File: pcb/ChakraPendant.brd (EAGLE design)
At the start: 25.4 x 25.4 mm, 12 parts

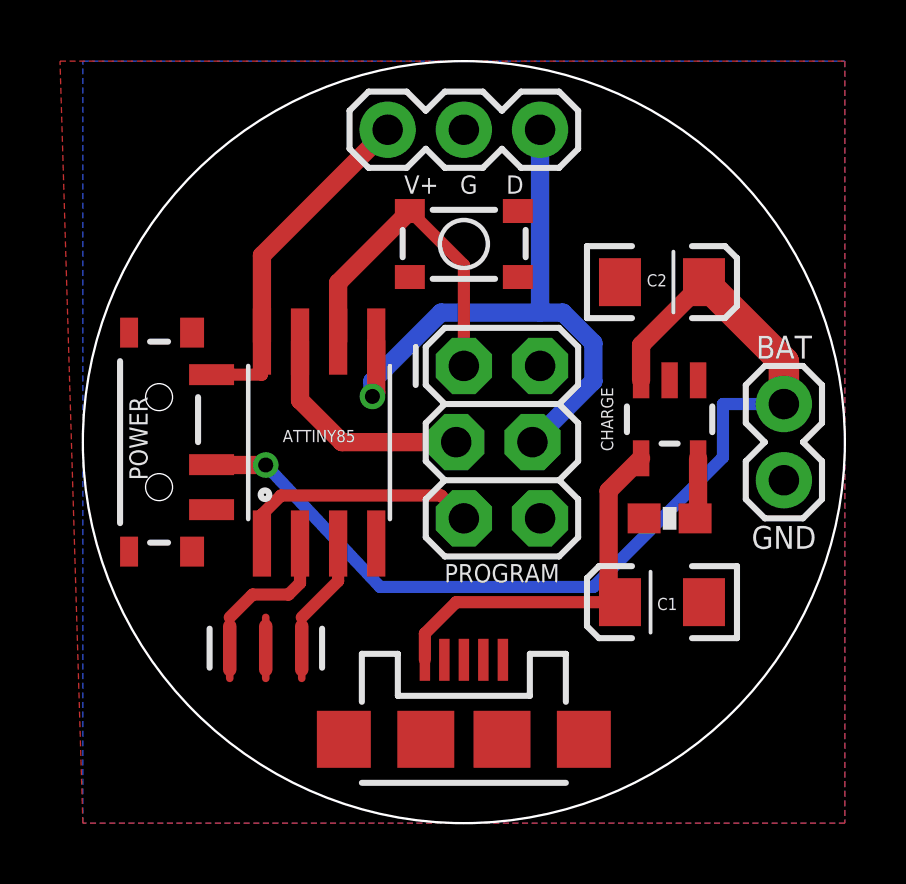
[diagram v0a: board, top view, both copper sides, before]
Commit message: Remove power switches. Add Charge LEDs. Change ISP header to pogopin programmer.
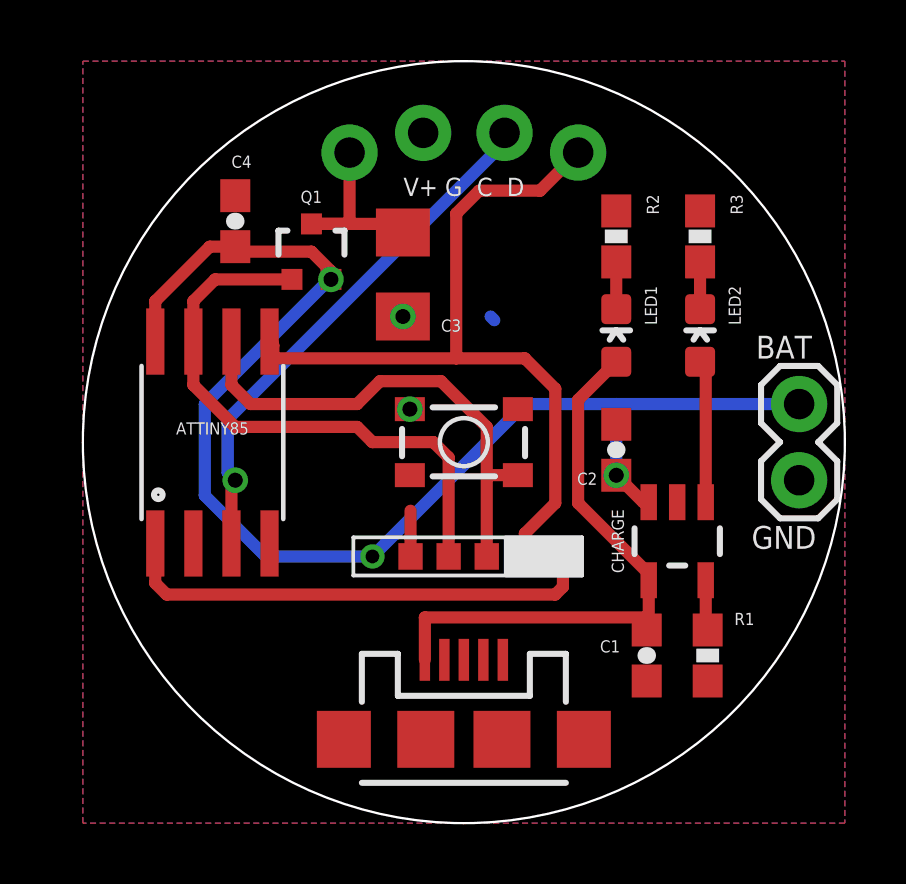
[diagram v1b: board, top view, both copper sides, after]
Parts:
- removed LEDS: (no value), SparkFun-Connectors:1X03
- removed MODE: SWITCH-MOMENTARY-2SMD-3, SparkFun-Electromechanical:TACTILE_SWITCH_SMD-3
- removed POWER: (no value), SparkFun-Electromechanical:SWITCH-SPST-SMD-A
- removed PROGRAM: (no value), SparkFun-Connectors:2X3_LOCK
- removed XTAL: 8MHZ, SparkFun-FreqCtrl:RESONATOR-SMD
- added C3: 22 uF, SparkFun-Passives:1206
- added C4: (no value), SparkFun-Passives:0603-CAP
- added LED1, LED2: (no value), SparkFun-LED:LED-0603
- added LEDPWR, LEDSIG: M021X02_NO_SILK, SparkFun-Connectors:1X02_NO_SILK
- added Q1: MOSFET-NCHANNEL2N7002PW, SparkFun-DiscreteSemi:SOT323
- added R2, R3: (no value), SparkFun-Passives:0603-RES
- added S2: SWITCH-MOMENTARY-2SMD-3, SparkFun-Electromechanical:TACTILE_SWITCH_SMD-3
- added U$1: POGOPIN-CONNWITHVIAS, Protofusion:POGOPROG-CONN-0H
- C1, C2: value 47 uF -> 4.7 uF; device SparkFun-Capacitors:EIA3216 -> SparkFun-Passives:0603-CAP
- moved C2 5.79 mm to (17.8, 12.4), turned to 90 degrees
- moved R1 4.75 mm to (20.8, 5.59), turned to 270 degrees
- moved CHARGE 4.07 mm to (19.8, 9.40)
- moved ATTINY85 3.56 mm to (4.32, 12.7)
- moved C1 1.85 mm to (18.8, 5.59), turned to 270 degrees
- moved BAT 0.51 mm to (23.9, 11.4)
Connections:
- removed net USBV+: C1.A, CHARGE.4, JP1.VBUS
- removed net VCC: ATTINY85.8, LEDS.1, POWER.3
- removed net XTAL1: ATTINY85.3, XTAL.1
- removed net XTAL2: ATTINY85.2, XTAL.3
- new net N$1: C3.1, LEDPWR.1, Q1.3
- new net N$2: C1.1, CHARGE.4, JP1.VBUS, LED1.A
- new net N$3: ATTINY85.3, LEDSIG.2
- new net N$4: LED1.C, R2.2
- new net N$5: LED2.C, R3.2
- new net N$7: CHARGE.1, LED2.A
- net BATTV+: now also ATTINY85.8, C2.1, C4.1, Q1.2, U$1.6; no longer C2.A, POWER.2
- net GND: now also C1.2, C2.2, C3.2, C4.2, LEDPWR.2, R2.1, R3.1, S2.4, U$1.5; no longer C1.C, C2.C, LEDS.2, MODE.4, PROGRAM.6, XTAL.2
- net PB0-MOSI: now also LEDSIG.1, U$1.2; no longer LEDS.3, PROGRAM.4
- net PB1-MISO: now also S2.1, U$1.3; no longer MODE.1, PROGRAM.1
- net PB2-SCK: now also Q1.1, U$1.4; no longer PROGRAM.3
- net PB5-RESET: now also U$1.1; no longer PROGRAM.5
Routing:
- net N$2: track 0.00 -> 19.7 mm
- net N$3: track 0.00 -> 17.7 mm, vias 0 -> 1
- net USBV+: track 13.2 -> 0.00 mm
- net VCC: track 11.6 -> 0.00 mm
- net PB2-SCK: track 7.74 -> 19.2 mm
- net BATTV+: track 33.7 -> 44.2 mm, vias 1 -> 2
- net PB5-RESET: track 8.27 -> 16.2 mm
- net N$1: track 0.00 -> 6.98 mm
- net PB1-MISO: track 11.3 -> 17.0 mm
- net PB0-MOSI: track 21.4 -> 27.0 mm, vias 1 -> 0
- net N$7: track 0.00 -> 4.76 mm
- net XTAL2: track 4.14 -> 0.00 mm
- net XTAL1: track 2.97 -> 0.00 mm
- net GND: track 0.00 -> 1.70 mm, vias 0 -> 2
- net N$5: track 0.00 -> 1.57 mm
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- added copper zone on layer 16, net GND
- removed copper zone on layer 16, net BATTV+
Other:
- board text added: "Chakra Pendant"
- board text added: "V+ G C D"
- board text added: "for Mom <3 Alex"
- board text added: "v4 Jan 7 2015"
- board text removed: "V+ G D"
- board text removed: "for Mom <3 your son Alex"

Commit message: Flip the terminals, because they will be mirrored.
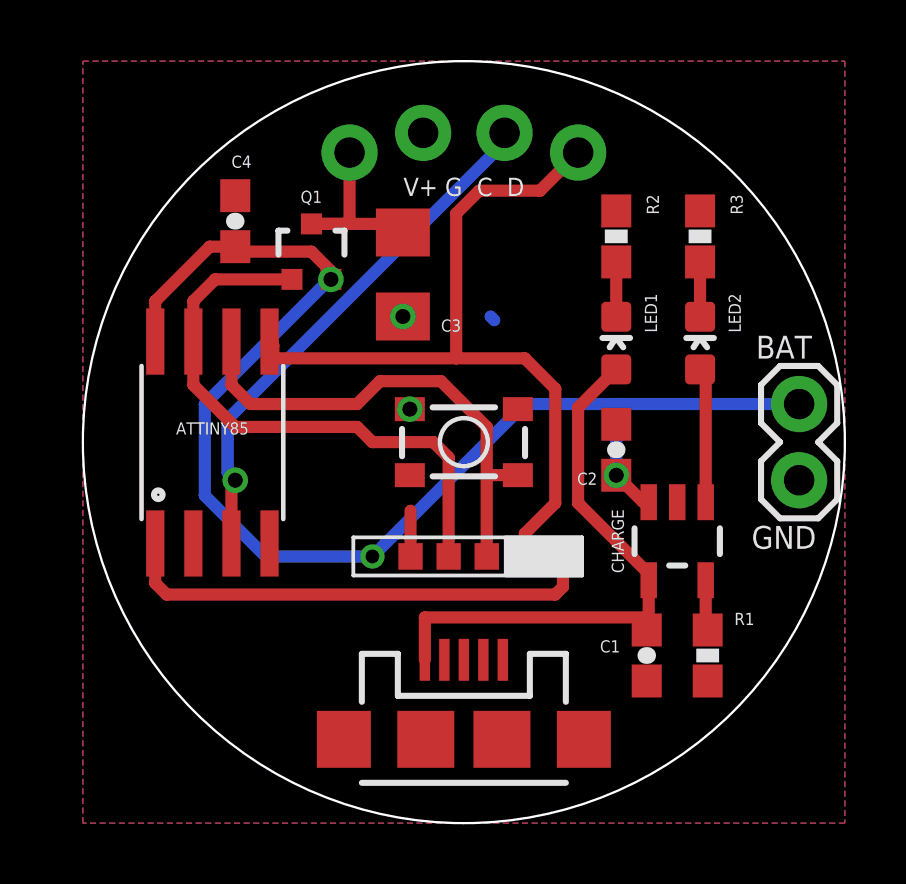
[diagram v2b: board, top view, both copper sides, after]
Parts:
- moved LED1 0.25 mm to (17.8, 16.0)
- moved LED2 0.25 mm to (20.6, 16.0)
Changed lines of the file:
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@@
 <layers>
 <layer number="1" name="Top" color="4" fill="1" visible="yes" active="yes"/>
-<layer number="16" name="Bottom" color="1" fill="1" visible="no" active="yes"/>
+<layer number="16" name="Bottom" color="1" fill="1" visible="yes" active="yes"/>
 <layer number="17" name="Pads" color="2" fill="1" visible="yes" active="yes"/>
 <layer number="18" name="Vias" color="2" fill="1" visible="yes" active="yes"/>
-<layer number="19" name="Unrouted" color="6" fill="1" visible="no" active="yes"/>
+<layer number="19" name="Unrouted" color="6" fill="1" visible="yes" active="yes"/>
 <layer number="20" name="Dimension" color="15" fill="1" visible="yes" active="yes"/>
 <layer number="21" name="tPlace" color="7" fill="1" visible="yes" active="yes"/>
-<layer number="22" name="bPlace" color="7" fill="1" visible="no" active="yes"/>
+<layer number="22" name="bPlace" color="7" fill="1" visible="yes" active="yes"/>
 <layer number="23" name="tOrigins" color="15" fill="1" visible="yes" active="yes"/>
-<layer number="24" name="bOrigins" color="15" fill="1" visible="no" active="yes"/>
+<layer number="24" name="bOrigins" color="15" fill="1" visible="yes" active="yes"/>
 <layer number="25" name="tNames" color="7" fill="1" visible="yes" active="yes"/>
-<layer number="26" name="bNames" color="7" fill="1" visible="no" active="yes"/>
+<layer number="26" name="bNames" color="7" fill="1" visible="yes" active="yes"/>
 <layer number="27" name="tValues" color="7" fill="1" visible="no" active="yes"/>
 <layer number="28" name="bValues" color="7" fill="1" visible="no" active="yes"/>
@@
 <attribute name="VALUE" x="18.558475" y="25.090109375" size="1.27" layer="27" rot="R165"/>
 </element>
-<element name="LED1" library="SparkFun-LED" package="LED-0603" value="" x="17.78" y="16.256" smashed="yes">
-<attribute name="NAME" x="18.7325" y="17.907" size="0.4064" layer="25" rot="R270"/>
-<attribute name="VALUE" x="18.8595" y="15.24" size="0.4064" layer="27" rot="R90"/>
-</element>
-<element name="LED2" library="SparkFun-LED" package="LED-0603" value="" x="20.574" y="16.256" smashed="yes">
-<attribute name="NAME" x="21.5265" y="17.907" size="0.4064" layer="25" rot="R270"/>
-<attribute name="VALUE" x="21.6535" y="15.24" size="0.4064" layer="27" rot="R90"/>
+<element name="LED1" library="SparkFun-LED" package="LED-0603" value="" x="17.78" y="16.002" smashed="yes">
+<attribute name="NAME" x="18.7325" y="17.653" size="0.4064" layer="25" rot="R270"/>
+<attribute name="VALUE" x="18.8595" y="14.986" size="0.4064" layer="27" rot="R90"/>
+</element>
+<element name="LED2" library="SparkFun-LED" package="LED-0603" value="" x="20.574" y="16.002" smashed="yes">
+<attribute name="NAME" x="21.5265" y="17.653" size="0.4064" layer="25" rot="R270"/>
+<attribute name="VALUE" x="21.6535" y="14.986" size="0.4064" layer="27" rot="R90"/>
 </element>
 <element name="R2" library="SparkFun-Passives" package="0603-RES" value="" x="17.78" y="19.558" smashed="yes" rot="R270">
@@
 <wire x1="18.862" y1="8.0979" x2="18.862" y2="8.316" width="0.4064" layer="1"/>
 <wire x1="18.862" y1="8.316" x2="16.51" y2="10.668" width="0.4064" layer="1"/>
-<wire x1="16.51" y1="10.668" x2="16.51" y2="14.109" width="0.4064" layer="1"/>
-<wire x1="16.51" y1="14.109" x2="17.78" y2="15.379" width="0.4064" layer="1"/>
+<wire x1="16.51" y1="10.668" x2="16.51" y2="13.855" width="0.4064" layer="1"/>
+<wire x1="16.51" y1="13.855" x2="17.78" y2="15.125" width="0.4064" layer="1"/>
 </signal>
 <signal name="N$3">
@@
 <contactref element="LED1" pad="C"/>
 <contactref element="R2" pad="2"/>
-<wire x1="17.78" y1="17.133" x2="17.78" y2="18.708" width="0.4064" layer="1"/>
+<wire x1="17.78" y1="16.879" x2="17.78" y2="18.708" width="0.4064" layer="1"/>
 </signal>
 <signal name="N$5">
 <contactref element="LED2" pad="C"/>
 <contactref element="R3" pad="2"/>
-<wire x1="20.574" y1="17.133" x2="20.574" y2="18.708" width="0.4064" layer="1"/>
+<wire x1="20.574" y1="16.879" x2="20.574" y2="18.708" width="0.4064" layer="1"/>
 </signal>
 <signal name="N$7">
 <contactref element="CHARGE" pad="1"/>
 <contactref element="LED2" pad="A"/>
-<wire x1="20.574" y1="15.379" x2="20.762" y2="15.191" width="0.4064" layer="1"/>
+<wire x1="20.574" y1="15.125" x2="20.762" y2="15.191" width="0.4064" layer="1"/>
 <wire x1="20.762" y1="15.191" x2="20.762" y2="10.6981" width="0.4064" layer="1"/>
 </signal>

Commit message: GREATLY cleaned up main board schematic. Piped charge STAT to chip
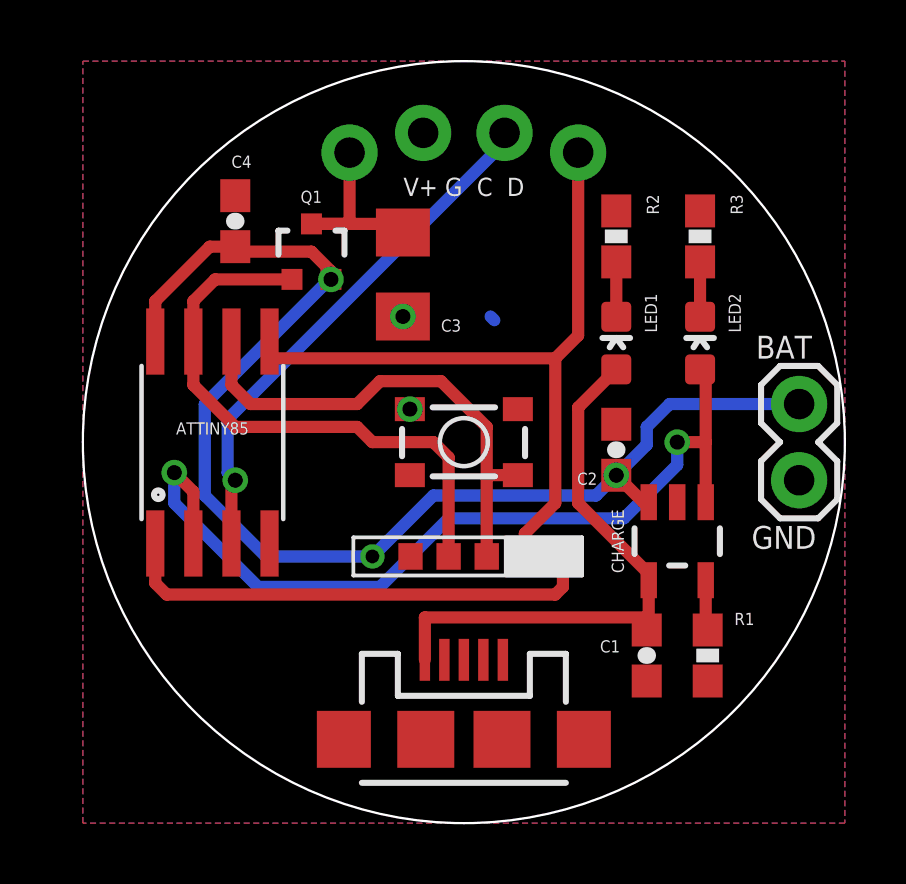
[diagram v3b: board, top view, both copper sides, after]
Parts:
- added FRAME1: FRAME-LETTER, SparkFun-Aesthetics:CREATIVE_COMMONS
- C4: value (none) -> 0.1 uF
- LED1: value (none) -> Amber
- LED2: value (none) -> Green
- R2, R3: value (none) -> 220
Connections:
- net BATTV+ renamed +4.1V
- net N$2 renamed USB5V
- removed net N$7: CHARGE.1, LED2.A
- new net PB3-ADC3: ATTINY85.2, CHARGE.1, LED2.A
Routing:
- net PB3-ADC3: track 0.00 -> 29.6 mm, vias 0 -> 2
- net N$7: track 4.69 -> 0.00 mm
- net PB0-MOSI: track 27.0 -> 24.3 mm
- net +4.1V: track 44.2 -> 42.2 mm
- net GND: track 1.70 -> 0.18 mm

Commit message: Fix that MOSFET was wired backwards :(
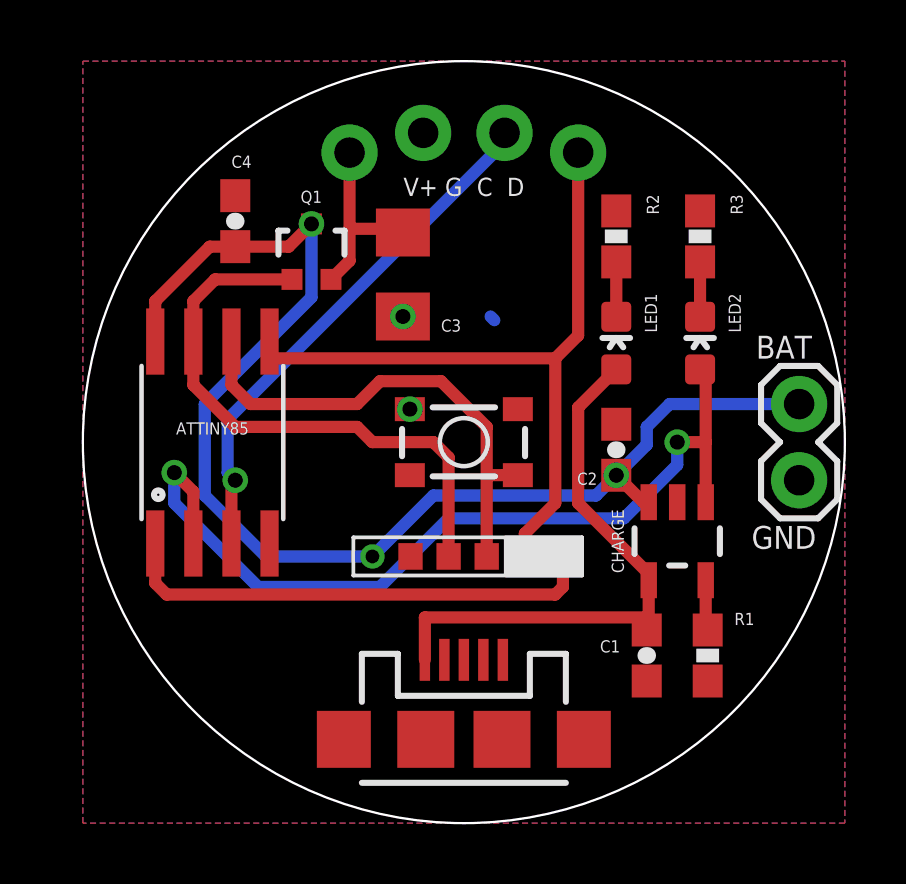
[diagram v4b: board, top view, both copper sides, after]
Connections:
- net +4.1V: now also Q1.3; no longer Q1.2
- net N$1: now also Q1.2; no longer Q1.3
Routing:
- net +4.1V: track 42.2 -> 42.9 mm
- net N$1: track 6.98 -> 6.31 mm
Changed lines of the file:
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@@
 <contactref element="CHARGE" pad="3"/>
 <contactref element="ATTINY85" pad="8"/>
-<contactref element="Q1" pad="2"/>
 <contactref element="C2" pad="1"/>
 <contactref element="BAT" pad="2"/>
 <contactref element="U$1" pad="6"/>
 <contactref element="C4" pad="1"/>
-<via x="8.27" y="18.125" extent="1-16" drill="0.5"/>
 <via x="17.78" y="11.596" extent="1-16" drill="0.5"/>
 <wire x1="18.862" y1="10.6981" x2="18.6779" y2="10.6981" width="0.4064" layer="1"/>
@@
 <wire x1="2.413" y1="17.399" x2="4.23" y2="19.216" width="0.4064" layer="1"/>
 <wire x1="4.23" y1="19.216" x2="5.08" y2="19.216" width="0.4064" layer="1"/>
-<wire x1="8.27" y1="18.125" x2="8.27" y2="18.4" width="0.4064" layer="1"/>
-<wire x1="8.27" y1="18.4" x2="7.62" y2="19.05" width="0.4064" layer="1"/>
-<wire x1="7.62" y1="19.05" x2="5.08" y2="19.05" width="0.4064" layer="1"/>
 <wire x1="5.08" y1="19.05" x2="5.08" y2="19.216" width="0.4064" layer="1"/>
-<wire x1="8.27" y1="18.125" x2="8.219" y2="18.125" width="0.4064" layer="16"/>
-<wire x1="8.219" y1="18.125" x2="4.064" y2="13.97" width="0.4064" layer="16"/>
 <wire x1="4.064" y1="13.97" x2="4.064" y2="10.922" width="0.4064" layer="16"/>
 <wire x1="4.064" y1="10.922" x2="6.096" y2="8.89" width="0.4064" layer="16"/>
@@
 <wire x1="18.796" y1="13.208" x2="18.796" y2="12.612" width="0.4064" layer="16"/>
 <wire x1="18.796" y1="12.612" x2="17.78" y2="11.596" width="0.4064" layer="16"/>
+<contactref element="Q1" pad="3"/>
+<wire x1="4.064" y1="13.97" x2="7.62" y2="17.526" width="0.4064" layer="16"/>
+<wire x1="7.62" y1="17.526" x2="7.62" y2="19.975" width="0.4064" layer="16"/>
+<via x="7.62" y="19.975" extent="1-16" drill="0.5"/>
+<wire x1="5.08" y1="19.216" x2="6.861" y2="19.216" width="0.4064" layer="1"/>
+<wire x1="6.861" y1="19.216" x2="7.62" y2="19.975" width="0.4064" layer="1"/>
 </signal>
 <signal name="PB2-SCK">
@@
 </signal>
 <signal name="N$1" class="1">
-<contactref element="Q1" pad="3"/>
 <contactref element="C3" pad="1"/>
 <contactref element="LEDPWR" pad="1"/>
-<wire x1="8.89" y1="22.352" x2="8.89" y2="19.975" width="0.4064" layer="1"/>
-<wire x1="8.89" y1="19.975" x2="7.62" y2="19.975" width="0.4064" layer="1"/>
-<wire x1="7.62" y1="19.975" x2="10.668" y2="19.975" width="0.4064" layer="1"/>
-<wire x1="10.668" y1="19.975" x2="10.668" y2="19.688" width="0.4064" layer="1"/>
+<contactref element="Q1" pad="2"/>
+<wire x1="8.27" y1="18.125" x2="8.89" y2="18.745" width="0.4064" layer="1"/>
+<wire x1="8.89" y1="18.745" x2="8.89" y2="19.812" width="0.4064" layer="1"/>
+<wire x1="8.89" y1="19.812" x2="8.89" y2="22.352" width="0.4064" layer="1"/>
+<wire x1="10.668" y1="19.688" x2="10.544" y2="19.812" width="0.4064" layer="1"/>
+<wire x1="10.544" y1="19.812" x2="8.89" y2="19.812" width="0.4064" layer="1"/>
 </signal>
 <signal name="USB5V" class="1">

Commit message: Swap clock and data. Oops.
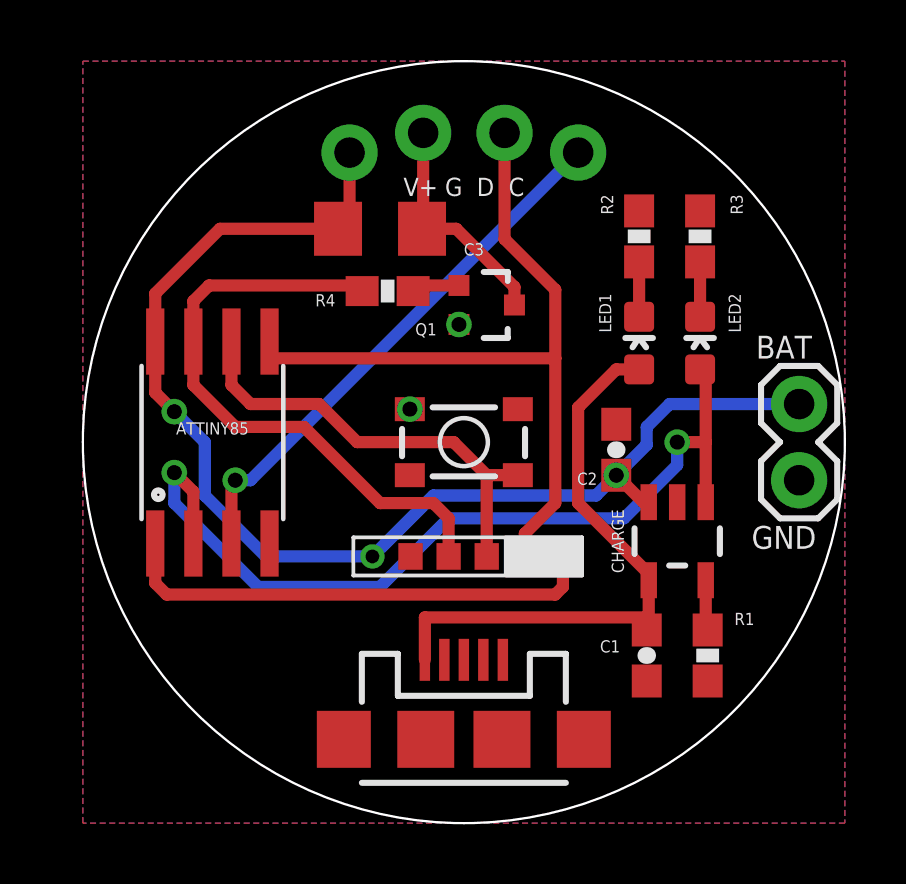
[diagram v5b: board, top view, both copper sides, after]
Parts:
- removed C4: 0.1 uF, SparkFun-Passives:0603-CAP
- added R4: 220, SparkFun-Passives:0603-RES
- moved Q1 6.11 mm to (13.5, 17.3), turned to 270 degrees
- moved C3 1.70 mm to (9.91, 19.8), turned to 0 degrees
- moved LED1 0.76 mm to (18.5, 16.0)
- moved R2 0.76 mm to (18.5, 19.6)
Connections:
- new net N$2: C3.2, LEDPWR.2, Q1.3
- net +4.1V: now also C3.1, LEDPWR.1; no longer C4.1, Q1.3
- net GND: now also Q1.2; no longer C3.2, C4.2, LEDPWR.2
- net N$1: now also Q1.1, R4.2; no longer C3.1, LEDPWR.1, Q1.2
- net N$3: now also LEDSIG.1; no longer LEDSIG.2
- net PB0-MOSI: now also LEDSIG.2; no longer LEDSIG.1
- net PB2-SCK: now also R4.1; no longer Q1.1
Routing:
- net N$2: track 0.00 -> 7.70 mm
- net N$1: track 6.31 -> 1.60 mm
- net PB1-MISO: track 17.0 -> 15.4 mm
- net +4.1V: track 42.9 -> 41.7 mm
- net PB2-SCK: track 19.2 -> 20.3 mm
- net PB0-MOSI: track 24.3 -> 25.3 mm
- net USB5V: track 19.4 -> 20.2 mm
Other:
- board text added: "/Users/alex/Projects/BeautifulPixel/Logo/Logo Line.bmp"
- board text added: "V+ G D C"
- board text added: "v5 Jan 21 2015"
- board text removed: "V+ G C D"
- board text removed: "v4 Jan 7 2015"
